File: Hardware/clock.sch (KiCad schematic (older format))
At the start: 25 parts

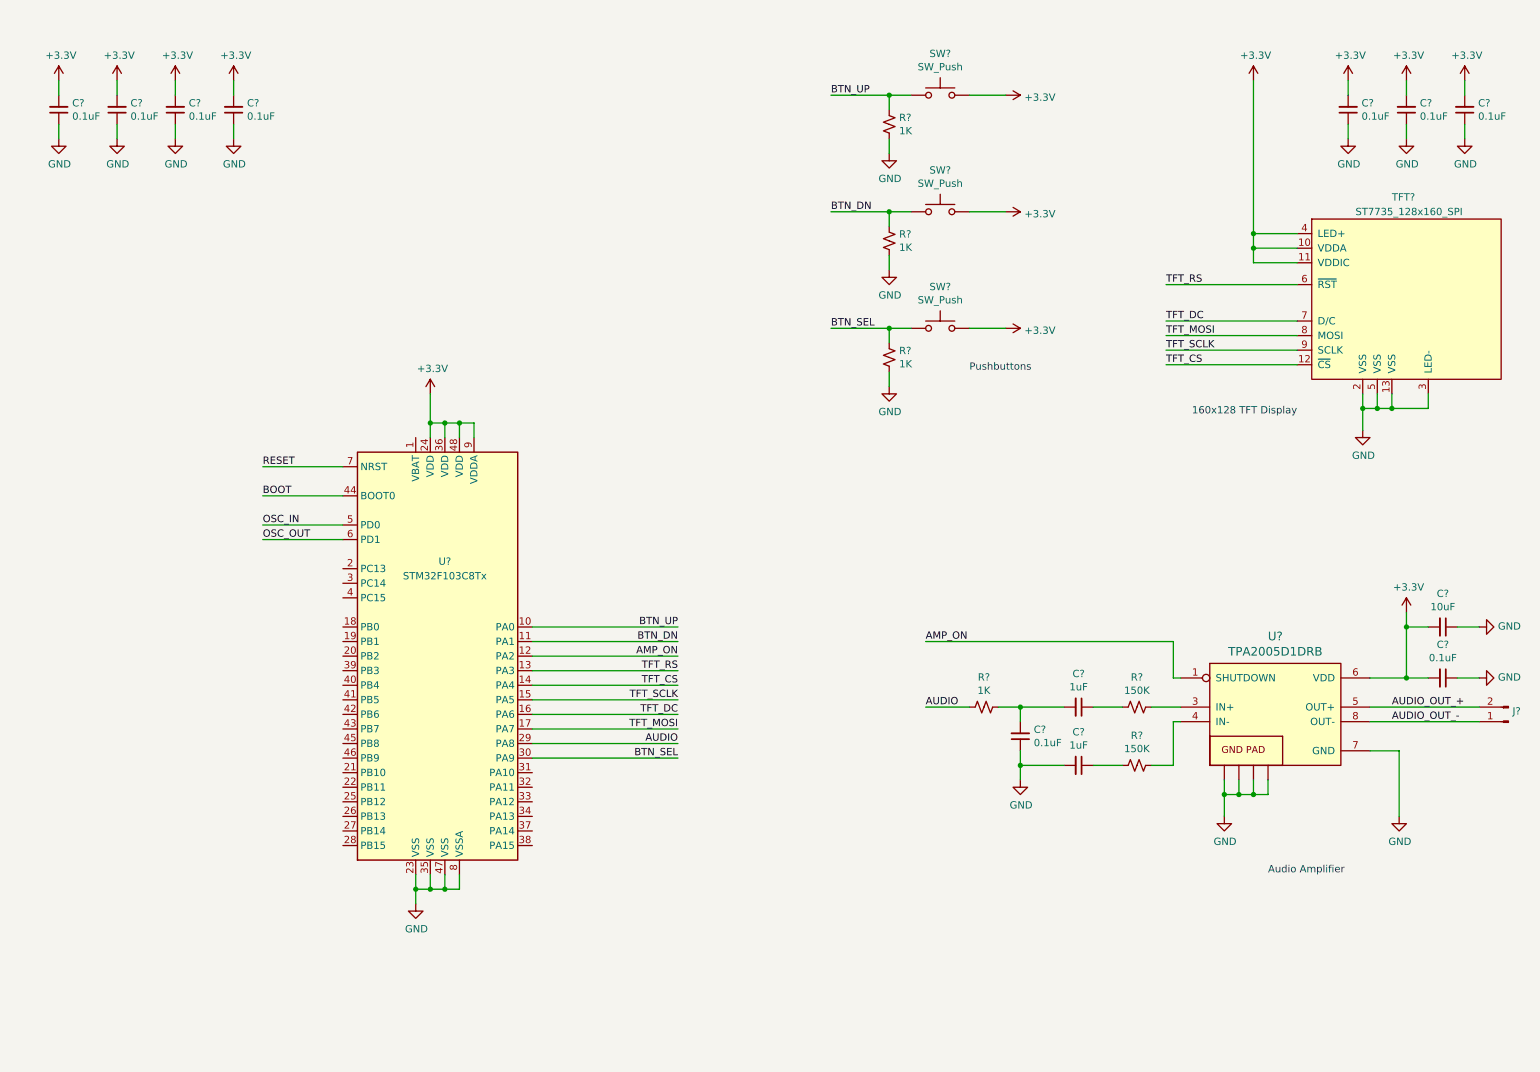
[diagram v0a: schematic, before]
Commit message: Changes to schematic. Implemented display dimming and menu items to control dimming.
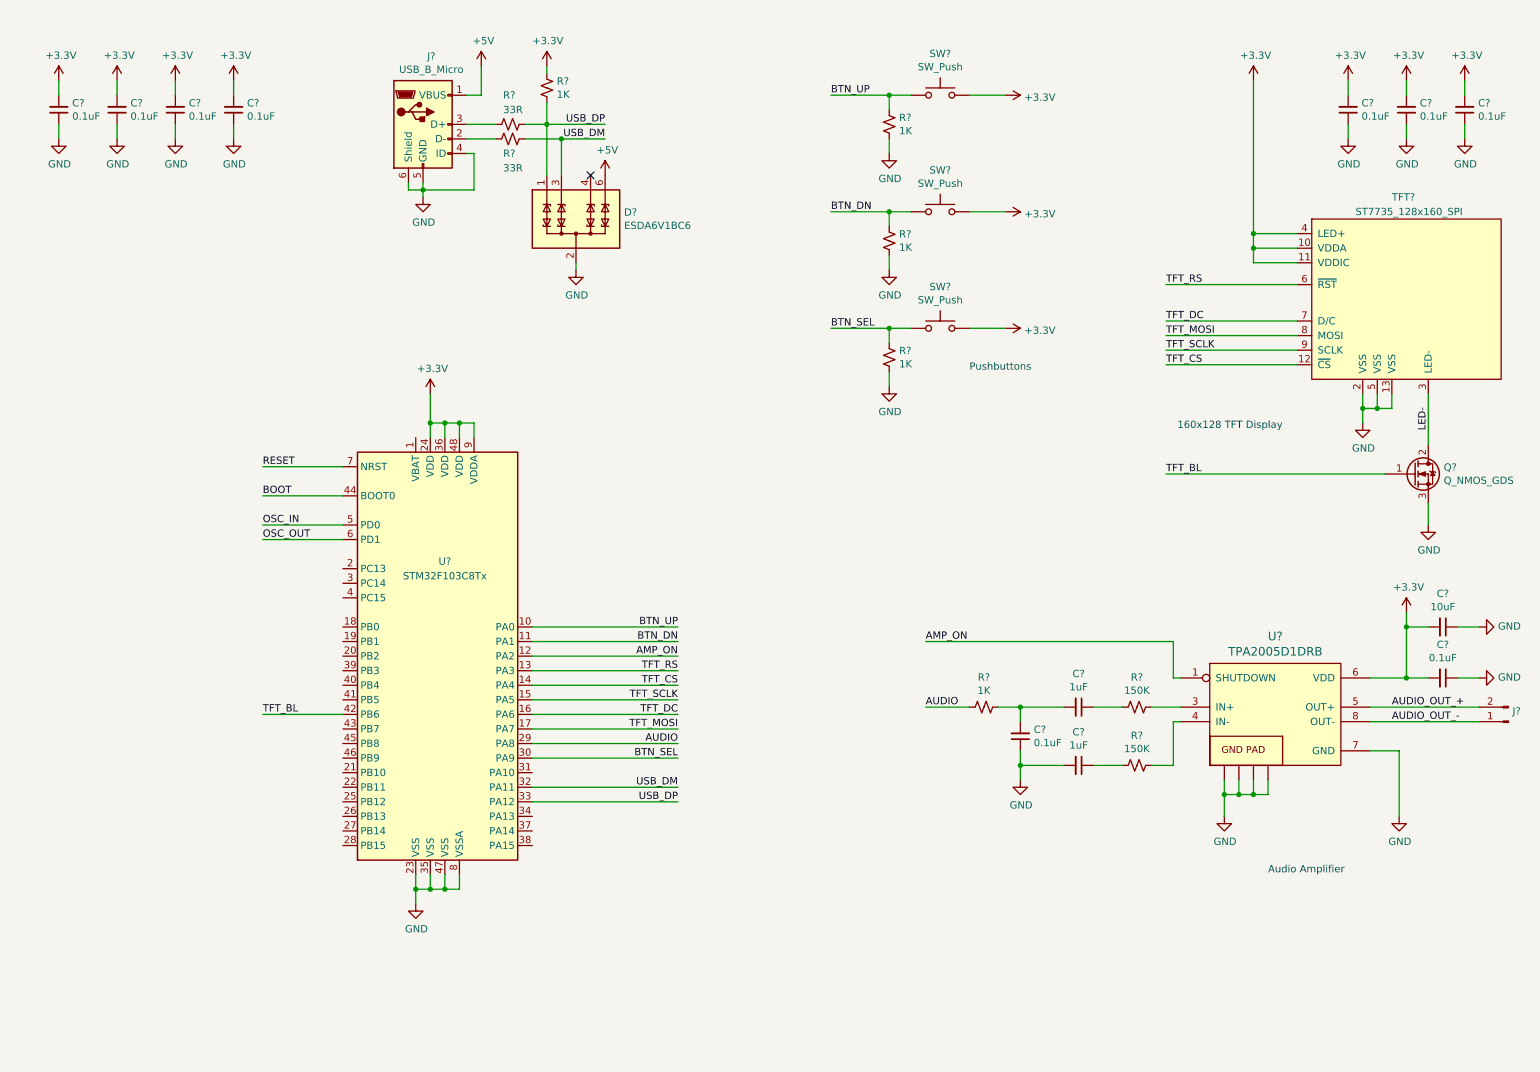
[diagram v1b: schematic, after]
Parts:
- added D?: ESDA6V1BC6, Package_TO_SOT_SMD:SOT-23-6, symbol Power_Protection:ESDA6V1BC6
- added J?: USB_B_Micro, symbol Connector:USB_B_Micro
- added Q?: Q_NMOS_GDS, symbol Device:Q_NMOS_GDS
- added R? (x2): 33R, symbol Device:R_Small_US
- added R?: 1K, symbol Device:R_Small_US
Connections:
- net +3V3: now also R?.2
- net GND: now also D?.2 (COM), D?.5 (COM), J?.4 (ID), J?.5 (GND), J?.6 (Shield), Q?.3 (S); no longer TFT?.3 (LED-)
- net USB_DM: now reaches U?.32 (PA11)
- net USB_DM: now also D?.3 (TVS2), R?.2
- net USB_DP: now reaches U?.33 (PA12)
- net USB_DP: now also D?.1 (TVS1), R?.1, R?.2
- net TFT_BL: now reaches U?.42 (PB6)
- net TFT_BL: now also Q?.1 (G)
- new net: J?.2 (D-), R?.1
- new net: J?.3 (D+), R?.1
- new net +5V: D?.6 (TVS4), J?.1 (VBUS)
- new net LED-: Q?.2 (D), TFT?.3 (LED-)
- no-connect marks 0 -> 1
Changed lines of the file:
@@
 L power:GND #PWR?
 U 1 1 5E2FD14C
-P 9800 3350
-F 0 "#PWR?" H 9800 3100 50  0001 C CNN
-F 1 "GND" H 9805 3177 50  0000 C CNN
-F 2 "" H 9800 3350 50  0001 C CNN
-F 3 "" H 9800 3350 50  0001 C CNN
-	1    9800 3350
+P 9800 3300
+F 0 "#PWR?" H 9800 3050 50  0001 C CNN
+F 1 "GND" H 9805 3127 50  0000 C CNN
+F 2 "" H 9800 3300 50  0001 C CNN
+F 3 "" H 9800 3300 50  0001 C CNN
+	1    9800 3300
 	1    0    0    -1
 $EndComp
@@
 	9800 3100 9800 3200
 Wire Wire Line
-	10250 3100 10250 3200
-Wire Wire Line
-	10250 3200 10000 3200
-Connection ~ 9800 3200
-Wire Wire Line
-	9800 3200 9800 3350
-Wire Wire Line
 	10000 3100 10000 3200
-Connection ~ 10000 3200
 Wire Wire Line
 	10000 3200 9900 3200
@@
 Wire Wire Line
 	10500 1350 10500 1250
-Text Notes 9350 3250 2    50   ~ 0
+Text Notes 9250 3350 2    50   ~ 0
 160x128 TFT Display
 $Comp
@@
 Wire Wire Line
 	9050 950  9050 2000
+$Comp
+L power:GND #PWR?
+U 1 1 5E4AE3AD
+P 10250 4000
+F 0 "#PWR?" H 10250 3750 50  0001 C CNN
+F 1 "GND" H 10255 3827 50  0000 C CNN
+F 2 "" H 10250 4000 50  0001 C CNN
+F 3 "" H 10250 4000 50  0001 C CNN
+	1    10250 4000
+	1    0    0    -1
+$EndComp
+$Comp
+L Device:Q_NMOS_GDS Q?
+U 1 1 5E4A6237
+P 10150 3650
+F 0 "Q?" H 10356 3696 50  0000 L CNN
+F 1 "Q_NMOS_GDS" H 10356 3605 50  0000 L CNN
+F 2 "" H 10350 3750 50  0001 C CNN
+F 3 "~" H 10150 3650 50  0001 C CNN
+	1    10150 3650
+	1    0    0    -1
+$EndComp
+Wire Wire Line
+	9800 3300 9800 3200
+Connection ~ 9800 3200
+Wire Wire Line
+	10250 3850 10250 4000
+Text Label 10250 3350 1    50   ~ 0
+LED-
+Wire Wire Line
+	10250 3100 10250 3450
+Wire Wire Line
+	8450 3650 9950 3650
+Text Label 8450 3650 0    50   ~ 0
+TFT_BL
+Wire Wire Line
+	2800 5300 2250 5300
+Text Label 2250 5300 0    50   ~ 0
+TFT_BL
+Wire Wire Line
+	4100 5800 5100 5800
+Wire Wire Line
+	4100 5900 5100 5900
+Text Label 5100 5800 2    50   ~ 0
+USB_DM
+Text Label 5100 5900 2    50   ~ 0
+USB_DP
+$Comp
+L Connector:USB_B_Micro J?
+U 1 1 5E4EA770
+P 3350 1250
+F 0 "J?" H 3407 1717 50  0000 C CNN
+F 1 "USB_B_Micro" H 3407 1626 50  0000 C CNN
+F 2 "" H 3500 1200 50  0001 C CNN
+F 3 "~" H 3500 1200 50  0001 C CNN
+	1    3350 1250
+	1    0    0    -1
+$EndComp
+$Comp
+L Device:R_Small_US R?
+U 1 1 5E4ED380
+P 3950 1250
+F 0 "R?" V 4150 1300 50  0000 R CNN
+F 1 "33R" V 4050 1300 50  0000 R CNN
+F 2 "" H 3950 1250 50  0001 C CNN
+F 3 "~" H 3950 1250 50  0001 C CNN
+	1    3950 1250
+	0    -1   -1   0
+$EndComp
+$Comp
+L Device:R_Small_US R?
+U 1 1 5E4EE10E
+P 3950 1350
+F 0 "R?" V 3850 1400 50  0000 R CNN
+F 1 "33R" V 3750 1400 50  0000 R CNN
+F 2 "" H 3950 1350 50  0001 C CNN
+F 3 "~" H 3950 1350 50  0001 C CNN
+	1    3950 1350
+	0    -1   -1   0
+$EndComp
+$Comp
+L power:GND #PWR?
+U 1 1 5E4EFB9D
+P 3350 1750
+F 0 "#PWR?" H 3350 1500 50  0001 C CNN
+F 1 "GND" H 3355 1577 50  0000 C CNN
+F 2 "" H 3350 1750 50  0001 C CNN
+F 3 "" H 3350 1750 50  0001 C CNN
+	1    3350 1750
+	1    0    0    -1
+$EndComp
+Wire Wire Line
+	3350 1750 3350 1700
+Wire Wire Line
+	3250 1650 3250 1700
+Wire Wire Line
+	3250 1700 3350 1700
+Connection ~ 3350 1700
+Wire Wire Line
+	3350 1700 3350 1650
+Wire Wire Line
+	3650 1450 3700 1450
+Wire Wire Line
+	3700 1450 3700 1700
+Wire Wire Line
+	3700 1700 3350 1700
+Wire Wire Line
+	3650 1250 3850 1250
+Wire Wire Line
+	3850 1350 3650 1350
+Wire Wire Line
+	4050 1250 4200 1250
+Wire Wire Line
+	4050 1350 4300 1350
+Text Label 4600 1250 2    50   ~ 0
+USB_DP
+Text Label 4600 1350 2    50   ~ 0
+USB_DM
+$Comp
+L power:+5V #PWR?
+U 1 1 5E51F126
+P 3750 850
+F 0 "#PWR?" H 3750 700 50  0001 C CNN
+F 1 "+5V" H 3765 1023 50  0000 C CNN
+F 2 "" H 3750 850 50  0001 C CNN
+F 3 "" H 3750 850 50  0001 C CNN
+	1    3750 850
+	1    0    0    -1
+$EndComp
+Wire Wire Line
+	3750 1050 3650 1050
+$Comp
+L Device:R_Small_US R?
+U 1 1 5E5253A7
+P 4200 1000
+F 0 "R?" H 4132 954 50  0000 R CNN
+F 1 "1K" H 4132 1045 50  0000 R CNN
+F 2 "" H 4200 1000 50  0001 C CNN
+F 3 "~" H 4200 1000 50  0001 C CNN
+	1    4200 1000
+	-1   0    0    1
+$EndComp
+$Comp
+L power:+3.3V #PWR?
+U 1 1 5E525FDE
+P 4200 850
+F 0 "#PWR?" H 4200 700 50  0001 C CNN
+F 1 "+3.3V" H 4100 1023 50  0000 L CNN
+F 2 "" H 4200 850 50  0001 C CNN
+F 3 "" H 4200 850 50  0001 C CNN
+	1    4200 850
+	1    0    0    -1
+$EndComp
+Wire Wire Line
+	4200 900  4200 850
+Wire Wire Line
+	4200 1100 4200 1250
+Connection ~ 4200 1250
+Wire Wire Line
+	4200 1250 4600 1250
+Wire Wire Line
+	3750 850  3750 1050
+$Comp
+L Power_Protection:ESDA6V1BC6 D?
+U 1 1 5E53FD31
+P 4400 1900
+F 0 "D?" H 4730 1946 50  0000 L CNN
+F 1 "ESDA6V1BC6" H 4730 1855 50  0000 L CNN
+F 2 "Package_TO_SOT_SMD:SOT-23-6" H 4400 1550 50  0001 C CNN
+F 3 "http://www.st.com/content/ccc/resource/technical/document/datasheet/21/07/21/e3/a8/df/42/a2/CD00001906.pdf/files/CD00001906.pdf/jcr:content/translations/en.CD00001906.pdf" V 4400 1900 50  0001 C CNN
+	1    4400 1900
+	1    0    0    -1
+$EndComp
+$Comp
+L power:+5V #PWR?
+U 1 1 5E5473CD
+P 4600 1600
+F 0 "#PWR?" H 4600 1450 50  0001 C CNN
+F 1 "+5V" H 4615 1773 50  0000 C CNN
+F 2 "" H 4600 1600 50  0001 C CNN
+F 3 "" H 4600 1600 50  0001 C CNN
+	1    4600 1600
+	1    0    0    -1
+$EndComp
+NoConn ~ 4500 1600
+Wire Wire Line
+	4200 1600 4200 1250
+Wire Wire Line
+	4300 1600 4300 1350
+Connection ~ 4300 1350
+Wire Wire Line
+	4300 1350 4600 1350
+$Comp
+L power:GND #PWR?
+U 1 1 5E5591F5
+P 4400 2250
+F 0 "#PWR?" H 4400 2000 50  0001 C CNN
+F 1 "GND" H 4405 2077 50  0000 C CNN
+F 2 "" H 4400 2250 50  0001 C CNN
+F 3 "" H 4400 2250 50  0001 C CNN
+	1    4400 2250
+	1    0    0    -1
+$EndComp
+Wire Wire Line
+	4400 2250 4400 2200
 $EndSCHEMATC

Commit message: Updated schematic
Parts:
- added BT?: Battery_Cell, Battery:BatteryHolder_Keystone_3000_1x12mm, symbol Device:Battery_Cell
- added C?: 330n, symbol Device:CP1_Small
- added C? (x2): 100n, symbol Device:C_Small
- added C? (x2): 12p?, symbol Device:C_Small
- added C? (x2): 100p?, symbol Device:C_Small
- added D? (x2): D_Schottky, symbol Device:D_Schottky
- added J?: Barrel_Jack, symbol Connector:Barrel_Jack
- added J?: Conn_02x05_Counter_Clockwise, symbol Connector_Generic:Conn_02x05_Counter_Clockwise
- added U?: UA78M33CDCY, Package_TO_SOT_SMD:SOT-223-3_TabPin2, symbol ua78m:UA78M33CDCY
- added Y?: 8M0, symbol Device:Crystal
- added Y?: 32k678, symbol Device:Crystal
- C?: value 10uF -> 10u
- C? (x9): value 0.1uF -> 100n
- C? (x2): value 1uF -> 1u
- R? (x2): value 150K -> 150k
- R? (x4): value 1K -> 1k
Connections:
- net +3V3: now also C?.2, J?.5 (Pin_5), U?.3 (OUT)
- net +5V: now also C?.1, D?.1 (K), D?.1 (K), U?.1 (IN); no longer J?.1 (VBUS)
- net GND: now also BT?.2 (-), C?.1, C?.1, C?.1, C?.1, C?.1, C?.2, C?.2, J?.2, J?.9 (Pin_9), U?.2 (GND)
- net OSC_IN: now also C?.2, Y?.1
- net OSC_OUT: now also C?.2, Y?.2
- net RESET: now also C?.1, J?.6 (Pin_6)
- net 3VB: now reaches U?.1 (VBAT)
- net 3VB: now also BT?.1 (+)
- net OSC32_IN: now reaches U?.3 (PC14)
- net OSC32_IN: now also C?.2, Y?.1
- net SWDIO: now reaches U?.34 (PA13)
- net SWDIO: now also J?.3 (Pin_3)
- net SWCLK: now reaches U?.37 (PA14)
- net SWCLK: now also J?.4 (Pin_4)
- net SWO: now reaches U?.39 (PB3)
- net SWO: now also J?.2 (Pin_2)
- net OSC32_OUT: now reaches U?.4 (PC15)
- net OSC32_OUT: now also C?.2, Y?.2
- net BOOT: no longer names the net of U?.44 (BOOT0)
- new net: D?.2 (A), J?.1 (VBUS)
- new net: D?.2 (A), J?.1
- no-connect marks 1 -> 22
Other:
- moved on the sheet: R?, U?

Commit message: Finished schematic. Begun routing. Added enclosure design files from vendor.
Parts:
- added FB1, FB2: BLM18PG471SN1D, Resistor_SMD:R_0603_1608Metric_Pad1.05x0.95mm_HandSolder, symbol Device:Ferrite_Bead_Small
- added R1: 10k, Resistor_SMD:R_0603_1608Metric, symbol Device:R_Small_US
- C1, C10, C11, C12, C13, C14, C15, C16, C18, C19, C3, C5, C6, C8: renamed from C?; footprint (none) -> Capacitor_SMD:C_0402_1005Metric
- C17: renamed from C?; footprint (none) -> Capacitor_SMD:C_0603_1608Metric_Pad1.05x0.95mm_HandSolder
- C2, C4: renamed from C?; value 12p? -> 27p; footprint (none) -> Capacitor_SMD:C_0402_1005Metric
- C7, C9: renamed from C?; value 100p? -> 15p; footprint (none) -> Capacitor_SMD:C_0402_1005Metric
- D1, D3: renamed from D?; value D_Schottky -> B0540W-7-F; footprint (none) -> Diode_SMD:D_SOD-123
- J1: renamed from J?; footprint (none) -> Connector_PinHeader_2.54mm:PinHeader_2x05_P2.54mm_Vertical; symbol Connector_Generic:Conn_02x05_Counter_Clockwise -> Connector_Generic:Conn_02x05_Odd_Even
- J2: renamed from J?; footprint (none) -> Connector_PinHeader_2.54mm:PinHeader_1x02_P2.54mm_Horizontal
- J3: renamed from J?; footprint (none) -> Connector_USB:USB_Micro-B_Molex_47346-0001
- J4: renamed from J?; footprint (none) -> Foodprints:PJ-102A
- Q1: renamed from Q?; value Q_NMOS_GDS -> 2N7002ET1G; footprint (none) -> Package_TO_SOT_SMD:SOT-23_Handsoldering; symbol Device:Q_NMOS_GDS -> Device:Q_NMOS_GSD
- R10, R2, R3, R4, R8, R9: renamed from R?; footprint (none) -> Resistor_SMD:R_0603_1608Metric
- R5, R6, R7: renamed from R?; value 1k -> 10k; footprint (none) -> Resistor_SMD:R_0603_1608Metric
- SW1, SW2, SW3: renamed from SW?; footprint (none) -> Button_Switch_SMD:SW_Push_1P1T_NO_6x6mm_H9.5mm
- TFT1: renamed from TFT?; footprint (none) -> SPE_IM120905001_FPC:TFT_160x120_14pin
- U3: renamed from U?; footprint (none) -> Package_SO:MSOP-8-1EP_3x3mm_P0.65mm_EP1.73x1.85mm; symbol tpa2005d1:TPA2005D1DRB -> tpa2005d1:TPA2005D1DGN
- Y1: renamed from Y?; footprint (none) -> Crystal:Crystal_HC49-U_Vertical
- Y2: renamed from Y?; footprint (none) -> Crystal:Crystal_SMD_3215-2Pin_3.2x1.5mm
- gave numbers to parts that had none: 4
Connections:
- net +3V3: now also J1.9 (Pin_9); no longer J1.5 (Pin_5)
- net AUDIO_OUT_+: now also FB2.2; no longer J2.2 (Pin_2)
- net AUDIO_OUT_-: now also FB1.2; no longer J2.1 (Pin_1)
- net GND: now also J1.4 (Pin_4), Q1.2 (S), U3.9 (GND@2), R1.1; no longer J1.9 (Pin_9), Q1.3 (S), U3.10 (GND), U3.11 (GND), U3.12 (GND), U3.13 (GND)
- net LED-: now also Q1.3 (D); no longer Q1.2 (D)
- net RESET: now also J1.10 (Pin_10); no longer J1.6 (Pin_6)
- net SWCLK: now also J1.7 (Pin_7); no longer J1.4 (Pin_4)
- net SWDIO: now also J1.5 (Pin_5); no longer J1.3 (Pin_3)
- net SWO: now also J1.3 (Pin_3); no longer J1.2 (Pin_2)
- net USB_DM: now also D2.1 (TVS1); no longer D2.3 (TVS2)
- net USB_DP: now also D2.3 (TVS2); no longer D2.1 (TVS1)
- net BOOT0: now reaches U1.44 (BOOT0)
- net BOOT0: now also R1.2
- new net: FB1.1, J2.1 (Pin_1)
- new net: FB2.1, J2.2 (Pin_2)
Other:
- moved on the sheet: J2
